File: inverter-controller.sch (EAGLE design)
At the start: 168 parts, among them IC1 STM32F334C8T6, IC10 ISO3082, IC2 SY7152ABC, IC3 LMV358MMX, IC4 LMV358MMX, IC5 SY7152ABC, J2 61300211121, J3 CONNECTOR-SMD-2PIN, J4 CONNECTOR-SMD-2PIN, J5 CONNECTOR-SMD-2PIN, X3 0289-9068**15EDGVC-3.81-03P-14, X6 1365-16, Y1 NX2016SA-32M

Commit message: Fan beslemelerinden 1 tanesi silindi, genisleme karti icin soket eklendi.
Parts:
- removed C56, C57, C64: 10nF, rcl:C-EUC0603E
- removed C58, C63: 100nF, rcl:C-EUC0603E
- removed C59, C62: 10uF, rcl:C-EUC0603E
- removed D5: 1119-3055, Diode:DIODEDO-214AC(SMA)
- removed IC5: SY7152ABC, SY7152ABC:SY7152ABC
- removed J5: CONNECTOR-SMD-2PIN, Andromeda:CONNECTOR-SMD-2PIN
- removed L2: 1319-4102**INDUCTOR POWER 22UH 4X4X1.8MM SMD, wuerth-elektronik:WE-PD2_S
- removed LED3: (no value), adafruit:LEDCHIP-LED0805
- removed R42: 1M, rcl:R-EU_R0603E
- removed R43: 200K, rcl:R-EU_R0603E
- removed R44: 10.5K, rcl:R-EU_R0603E
- removed R45, R46: 0R, rcl:R-EU_R0603E
- removed R47, R55: 1K, rcl:R-EU_R0603E
- removed R49, R50, R53: 33R, rcl:R-EU_R0603E
- added C65, C67: 100nF, rcl:C-EUC0603E
- added R57: (no value), rcl:R-EU_R0603E
- added U1: MCP9701, Texas Instruments - TMP235A4DBZR:TEXAS_INSTRUMENTS_TMP235A4DBZRTEXAS_INSTRUMENTS_TMP235A4DBZR_0_3
- added X1: 1365-10, con-leotronics:1365-10
- C54: value 10uF -> 100nF
- C55: value 100nF -> 10uF
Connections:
- net FAN1_EN renamed FAN_EN
- removed net +12V/2: C57.1, C58.1, C59.1, C62.1, D5.C, R43.1, R45.2, R46.2, R47.1
- removed net FAN2_EN: IC1.PB13, IC5.EN, R42.2
- removed net I_FAN1: C47.1, C48.1, R40.2
- removed net N$25: D5.A, IC5.LX, L2.1
- removed net N$26: IC5.FB, R43.2, R44.1
- removed net N$27: J5.1, R45.1, R46.1
- removed net N$28: J5.2, R49.1, R50.1, R53.1, R55.1
- removed net N$29: LED3.A, R47.2
- removed net NTC2: IC1.PB1
- new net CAN_RX: IC1.PB8, X1-3.S
- new net CAN_TX: IC1.PB9, X1-1.S
- new net EXTENSION_1: IC1.PB7, X1-5.S
- new net EXTENSION_2: IC1.PB6, X1-7.S
- new net EXTENSION_3: IC1.PB5, X1-9.S
- new net EXTENSION_4: IC1.PB4, X1-10.S
- new net EXTENSION_5: IC1.PA15, X1-6.S
- new net N$46: R57.2, U1.VOUT
- new net TAMB: C67.1, IC1.PB1, R57.1
- net +3V3: now also C54.2, C55.2, C65.1, U1.VDD, X1-4.S; no longer C54.1, C55.1, C56.1, IC5.IN, L2.2
- net GND: now also C54.1, C55.1, C65.2, C67.2, U1.GND, X1-2.S; no longer C54.2, C55.2, C56.2, C57.2, C58.2, C59.2, C62.2, C63.2, C64.2, IC5.GND, LED12.C, LED3.C, LED8.C, R42.1, R44.2, R49.2, R50.2, R53.2
- net I_FAN: now also C47.1, C48.1, R40.2; no longer C63.1, C64.1, R55.2
- net LED1: now also LED8.C
- net LED2: now also LED12.C
- net RS485_DIR: now also IC1.PB13; no longer IC1.PB5
- net RS485_LED: now also IC1.PC13; no longer IC1.PB4
- net RS485_RX: now also IC1.PB11; no longer IC1.PB7
- net RS485_TX: now also IC1.PB10; no longer IC1.PB6
- net SWO: now also X1-8.S
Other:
- note added: "Extension Board Header"
- moved on the sheet: C54, C55, JP1, LED12, LED8, R1, R36, R37

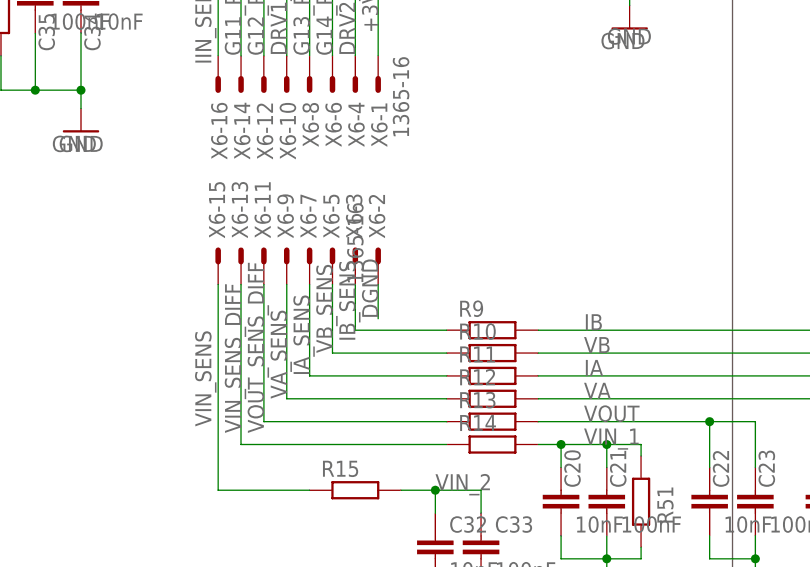
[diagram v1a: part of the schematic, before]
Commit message: Ana kart baglanti soketindeki GND baglanti sorunu giderildi(ERC).
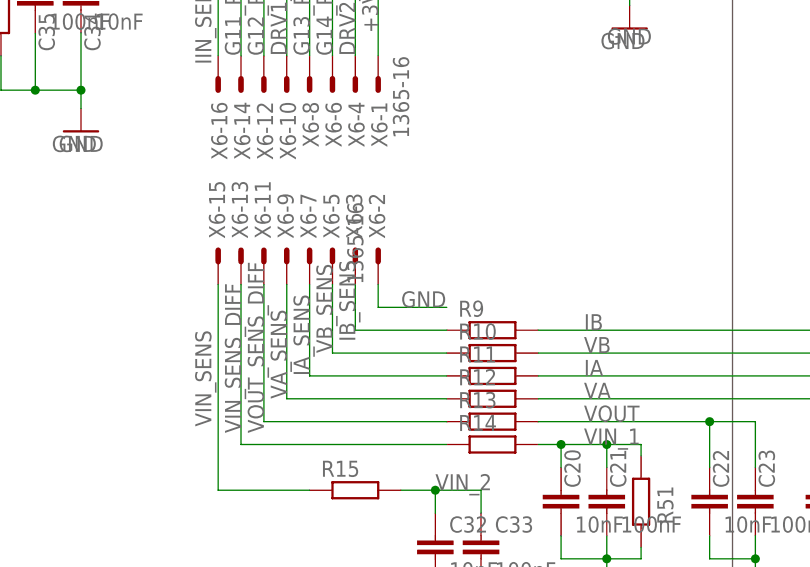
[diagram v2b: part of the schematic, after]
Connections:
- removed net DGND: X6-2.S
- net GND: now also X6-2.S
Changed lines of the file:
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@@
 <junction x="457.2" y="91.44"/>
+</segment>
+<segment>
+<pinref part="X6" gate="-2" pin="S"/>
+<wire x1="66.04" y1="213.36" x2="66.04" y2="210.82" width="0.1524" layer="91"/>
+<wire x1="66.04" y1="210.82" x2="73.66" y2="210.82" width="0.1524" layer="91"/>
+<label x="68.58" y="210.82" size="1.778" layer="95"/>
 </segment>
 </net>
@@
 <pinref part="R5" gate="G$1" pin="2"/>
 <pinref part="R6" gate="G$1" pin="1"/>
-</segment>
-</net>
-<net name="DGND" class="0">
-<segment>
-<label x="66.04" y="209.55" size="1.778" layer="95" rot="R90"/>
-<wire x1="66.04" y1="213.36" x2="66.04" y2="209.55" width="0.1524" layer="91"/>
-<pinref part="X6" gate="-2" pin="S"/>
 </segment>
 </net>
@@
 </sheet>
 </sheets>
+<errors>
+</errors>
 </schematic>
 </drawing>

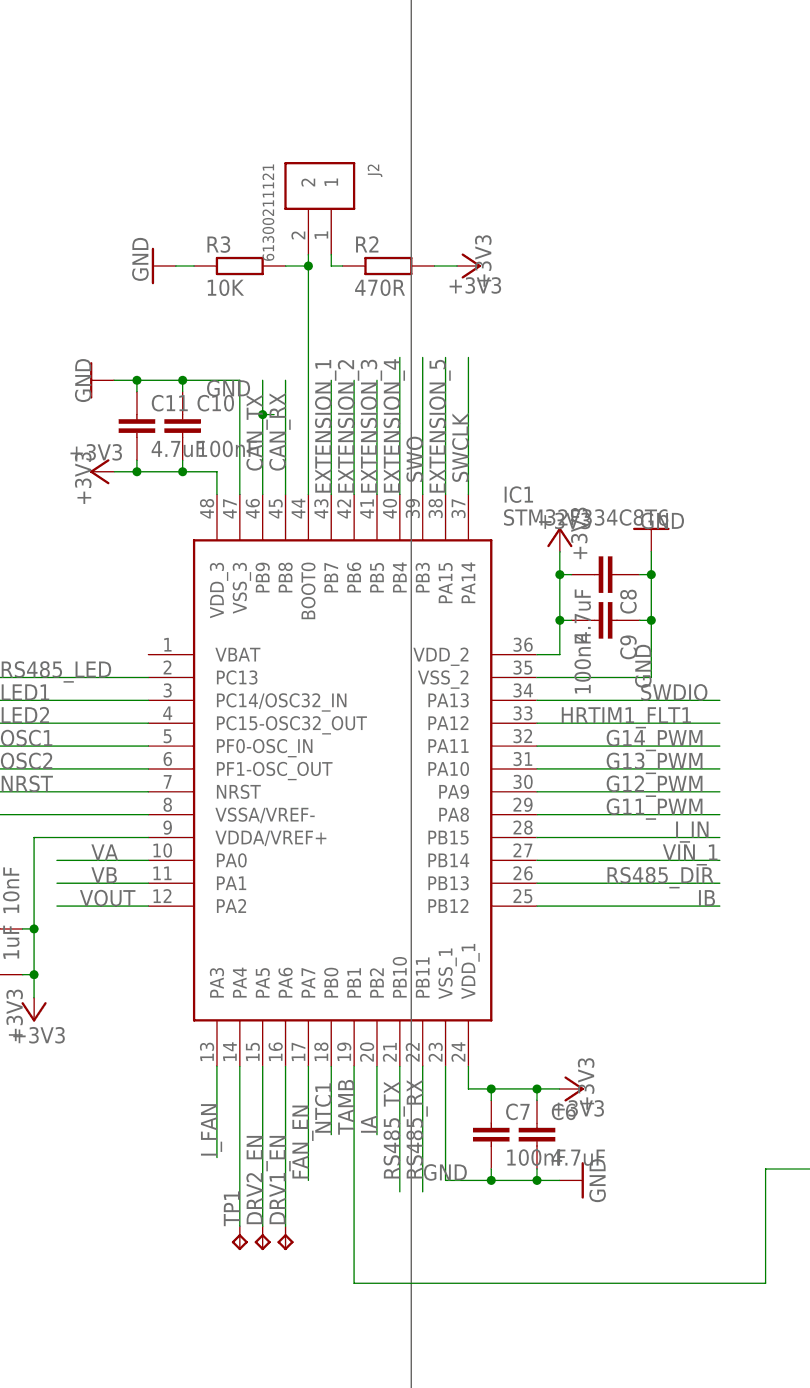
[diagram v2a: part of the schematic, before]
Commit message: NTC1 net ismi T_HEATSINK yapildi.
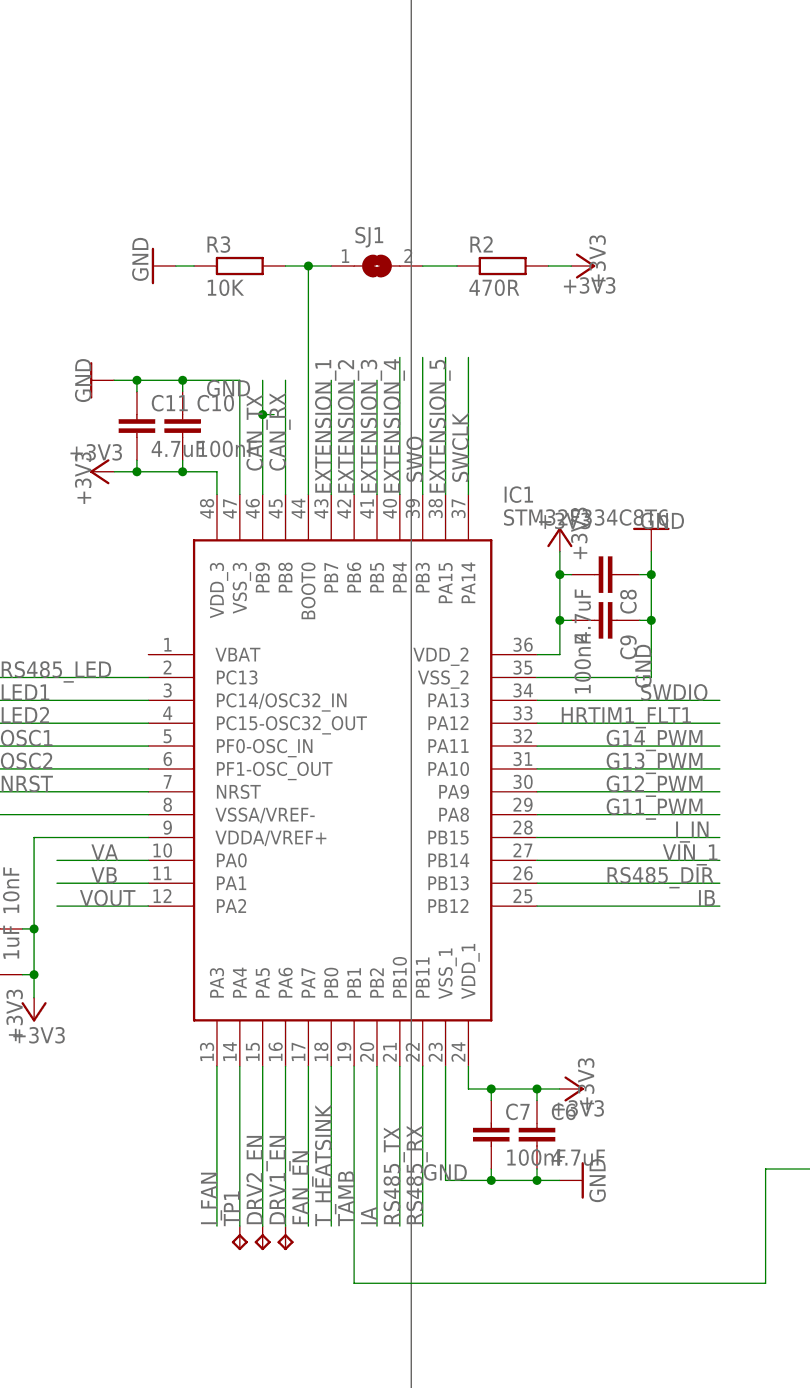
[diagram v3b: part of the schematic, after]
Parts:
- removed J2: 61300211121, Headers:61300211121
- added SJ1: (no value), jumper:SJ
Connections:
- new net T_HEATSINK: IC1.PB0
- net N$2: now also SJ1.2; no longer J2.1
- net N$6: now also SJ1.1; no longer J2.2
- net NTC1: no longer IC1.PB0
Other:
- moved on the sheet: R2
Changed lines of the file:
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@@
 <part name="+3V1" library="supply1" library_urn="urn:adsk.eagle:library:371" deviceset="+3V3" device=""/>
 <part name="Y1" library="enko" library_urn="urn:adsk.eagle:library:26809666" deviceset="NX2016SA-32M" device="" package3d_urn="urn:adsk.eagle:package:26812247/2"/>
-<part name="J2" library="Headers" library_urn="urn:adsk.eagle:library:11687645" deviceset="61300211121" device="" package3d_urn="urn:adsk.eagle:package:11390690/2"/>
 <part name="+3V2" library="supply1" library_urn="urn:adsk.eagle:library:371" deviceset="+3V3" device=""/>
 <part name="GND2" library="supply1" library_urn="urn:adsk.eagle:library:371" deviceset="GND" device=""/>
@@
 <part name="C54" library="rcl" library_urn="urn:adsk.eagle:library:26637914" deviceset="C-EU" device="C0603E" package3d_urn="urn:adsk.eagle:package:26638827/1" value="100nF"/>
 <part name="C55" library="rcl" library_urn="urn:adsk.eagle:library:26637914" deviceset="C-EU" device="C0603E" package3d_urn="urn:adsk.eagle:package:26638827/1" value="10uF"/>
+<part name="SJ1" library="jumper" library_urn="urn:adsk.eagle:library:252" deviceset="SJ" device="" package3d_urn="urn:adsk.eagle:package:15471/1"/>
 </parts>
 <sheets>
@@
 <wire x1="562.61" y1="128.27" x2="562.61" y2="276.86" width="0.6096" layer="125" style="shortdash"/>
 <wire x1="562.61" y1="276.86" x2="358.14" y2="276.86" width="0.6096" layer="125" style="shortdash"/>
-<text x="92.71" y="12.7" size="1.778" layer="125" rot="R90">ADC2_IN12/</text>
+<text x="92.71" y="2.54" size="1.778" layer="125" rot="R90">ADC2_IN12/</text>
 <text x="133.35" y="53.34" size="1.778" layer="125">/ADC2_IN13</text>
 <text x="133.35" y="58.42" size="1.778" layer="125">/ADC2_IN14</text>
 <text x="133.35" y="60.96" size="1.778" layer="125">/ADC2_IN15</text>
-<text x="87.63" y="12.7" size="1.778" layer="125" rot="R90">ADC1_IN11/</text>
-<text x="90.17" y="12.7" size="1.778" layer="125" rot="R90">ADC1_IN12/</text>
+<text x="87.63" y="2.54" size="1.778" layer="125" rot="R90">ADC1_IN11/</text>
+<text x="90.17" y="2.54" size="1.778" layer="125" rot="R90">ADC1_IN12/</text>
 <text x="365.76" y="113.03" size="5.08" layer="125">Extension Board Header</text>
 <wire x1="358.14" y1="120.65" x2="358.14" y2="58.42" width="0.6096" layer="125" style="shortdash"/>
@@
 <attribute name="VALUE" x="15.24" y="55.88" size="1.778" layer="96" rot="R90" align="center-left"/>
 </instance>
-<instance part="J2" gate="G$1" x="87.63" y="133.35" smashed="yes" rot="R270">
-<attribute name="NAME" x="91.694" y="135.89" size="1.27" layer="95" rot="R270"/>
-<attribute name="VALUE" x="80.01" y="135.89" size="1.27" layer="96" rot="R270"/>
-</instance>
-<instance part="+3V2" gate="G$1" x="104.14" y="124.46" smashed="yes" rot="R270">
-<attribute name="VALUE" x="106.68" y="123.19" size="1.778" layer="96" rot="R180"/>
+<instance part="+3V2" gate="G$1" x="116.84" y="124.46" smashed="yes" rot="R270">
+<attribute name="VALUE" x="119.38" y="123.19" size="1.778" layer="96" rot="R180"/>
 </instance>
 <instance part="GND2" gate="1" x="67.818" y="124.46" smashed="yes" rot="R270">
@@
 <attribute name="VALUE" x="13.97" y="93.218" size="1.778" layer="96"/>
 </instance>
-<instance part="R2" gate="G$1" x="93.98" y="124.46" smashed="yes">
-<attribute name="NAME" x="90.17" y="125.9586" size="1.778" layer="95"/>
-<attribute name="VALUE" x="90.17" y="121.158" size="1.778" layer="96"/>
+<instance part="R2" gate="G$1" x="106.68" y="124.46" smashed="yes">
+<attribute name="NAME" x="102.87" y="125.9586" size="1.778" layer="95"/>
+<attribute name="VALUE" x="102.87" y="121.158" size="1.778" layer="96"/>
 </instance>
 <instance part="R3" gate="G$1" x="77.47" y="124.46" smashed="yes">
@@
 <attribute name="VALUE" x="465.709" y="92.964" size="1.778" layer="96" rot="R90"/>
 </instance>
+<instance part="SJ1" gate="1" x="92.71" y="124.46" smashed="yes">
+<attribute name="NAME" x="90.17" y="127" size="1.778" layer="95"/>
+<attribute name="VALUE" x="90.17" y="120.65" size="1.778" layer="96"/>
+</instance>
 </instances>
 <busses>
@@
 <segment>
 <pinref part="+3V2" gate="G$1" pin="+3V3"/>
-<wire x1="101.6" y1="124.46" x2="99.06" y2="124.46" width="0.1524" layer="91"/>
-<label x="105.41" y="121.92" size="1.778" layer="95" rot="R90"/>
+<wire x1="114.3" y1="124.46" x2="111.76" y2="124.46" width="0.1524" layer="91"/>
+<label x="118.11" y="121.92" size="1.778" layer="95" rot="R90"/>
 <pinref part="R2" gate="G$1" pin="2"/>
 </segment>
@@
 <segment>
 <pinref part="IC1" gate="G$1" pin="PB2"/>
-<wire x1="92.71" y1="35.56" x2="92.71" y2="27.94" width="0.1524" layer="91"/>
-<label x="92.71" y="27.94" size="1.778" layer="95" rot="R90"/>
+<wire x1="92.71" y1="35.56" x2="92.71" y2="17.78" width="0.1524" layer="91"/>
+<label x="92.71" y="17.78" size="1.778" layer="95" rot="R90"/>
 </segment>
 <segment>
@@
 <net name="NTC1" class="0">
 <segment>
-<pinref part="IC1" gate="G$1" pin="PB0"/>
-<wire x1="87.63" y1="35.56" x2="87.63" y2="27.94" width="0.1524" layer="91"/>
-<label x="87.63" y="27.94" size="1.778" layer="95" rot="R90"/>
-</segment>
-<segment>
 <wire x1="248.92" y1="93.98" x2="245.11" y2="93.98" width="0.1524" layer="91"/>
 <wire x1="245.11" y1="93.98" x2="238.76" y2="93.98" width="0.1524" layer="91"/>
@@
 <pinref part="IC1" gate="G$1" pin="BOOT0"/>
 <wire x1="85.09" y1="99.06" x2="85.09" y2="124.46" width="0.1524" layer="91"/>
-<pinref part="J2" gate="G$1" pin="2"/>
 <pinref part="R3" gate="G$1" pin="2"/>
-<wire x1="85.09" y1="124.46" x2="85.09" y2="125.73" width="0.1524" layer="91"/>
 <wire x1="82.55" y1="124.46" x2="85.09" y2="124.46" width="0.1524" layer="91"/>
 <junction x="85.09" y="124.46"/>
+<pinref part="SJ1" gate="1" pin="1"/>
+<wire x1="87.63" y1="124.46" x2="85.09" y2="124.46" width="0.1524" layer="91"/>
 </segment>
 </net>
@@
 <net name="N$2" class="0">
 <segment>
-<pinref part="J2" gate="G$1" pin="1"/>
-<wire x1="88.9" y1="124.46" x2="87.63" y2="124.46" width="0.1524" layer="91"/>
-<wire x1="87.63" y1="124.46" x2="87.63" y2="125.73" width="0.1524" layer="91"/>
 <pinref part="R2" gate="G$1" pin="1"/>
+<pinref part="SJ1" gate="1" pin="2"/>
+<wire x1="101.6" y1="124.46" x2="97.79" y2="124.46" width="0.1524" layer="91"/>
 </segment>
 </net>
@@
 <segment>
 <pinref part="IC1" gate="G$1" pin="PA3"/>
-<wire x1="74.93" y1="35.56" x2="74.93" y2="25.4" width="0.1524" layer="91"/>
-<label x="74.93" y="25.4" size="1.778" layer="95" rot="R90"/>
+<wire x1="74.93" y1="35.56" x2="74.93" y2="17.78" width="0.1524" layer="91"/>
+<label x="74.93" y="17.78" size="1.778" layer="95" rot="R90"/>
 </segment>
 <segment>
@@
 <segment>
 <pinref part="IC1" gate="G$1" pin="PB10"/>
-<wire x1="95.25" y1="35.56" x2="95.25" y2="21.59" width="0.1524" layer="91"/>
-<label x="95.25" y="22.86" size="1.778" layer="95" rot="R90"/>
+<wire x1="95.25" y1="35.56" x2="95.25" y2="17.78" width="0.1524" layer="91"/>
+<label x="95.25" y="17.78" size="1.778" layer="95" rot="R90"/>
 </segment>
 </net>
@@
 <segment>
 <pinref part="IC1" gate="G$1" pin="PB11"/>
-<wire x1="97.79" y1="35.56" x2="97.79" y2="21.59" width="0.1524" layer="91"/>
-<label x="97.79" y="22.86" size="1.778" layer="95" rot="R90"/>
+<wire x1="97.79" y1="35.56" x2="97.79" y2="17.78" width="0.1524" layer="91"/>
+<label x="97.79" y="17.78" size="1.778" layer="95" rot="R90"/>
 </segment>
 </net>
@@
 <segment>
 <pinref part="IC1" gate="G$1" pin="PB1"/>
-<label x="90.17" y="27.94" size="1.778" layer="95" rot="R90"/>
+<label x="90.17" y="17.78" size="1.778" layer="95" rot="R90"/>
 <wire x1="90.17" y1="35.56" x2="90.17" y2="11.43" width="0.1524" layer="91"/>
 <wire x1="90.17" y1="11.43" x2="135.89" y2="11.43" width="0.1524" layer="91"/>
@@
 <segment>
 <pinref part="IC1" gate="G$1" pin="PA7"/>
-<wire x1="85.09" y1="35.56" x2="85.09" y2="22.86" width="0.1524" layer="91"/>
-<label x="85.09" y="22.86" size="1.778" layer="95" rot="R90"/>
+<wire x1="85.09" y1="35.56" x2="85.09" y2="17.78" width="0.1524" layer="91"/>
+<label x="85.09" y="17.78" size="1.778" layer="95" rot="R90"/>
 </segment>
 </net>
@@
 </segment>
 </net>
+<net name="T_HEATSINK" class="0">
+<segment>
+<pinref part="IC1" gate="G$1" pin="PB0"/>
+<wire x1="87.63" y1="35.56" x2="87.63" y2="17.78" width="0.1524" layer="91"/>
+<label x="87.63" y="17.78" size="1.778" layer="95" rot="R90"/>
+</segment>
+</net>
